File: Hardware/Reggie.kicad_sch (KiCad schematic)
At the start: 39 parts, among them J1 RBUS, U1 ESP32-S3, Y1 R940000171

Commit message: Updated connections
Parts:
- added R62: R, symbol Device:R
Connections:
- net GND: now also R62.2
- net VSPI_MOSI: now reaches U1.39 (GPIO34)
- net VSPI_MISO: now reaches U1.40 (GPIO35)
- net VSPI_SCLK: now reaches U1.41 (GPIO36)
- net BUCK_EN: now reaches U1.42 (GPIO37)
- net BuckPGOOD: now reaches U1.43 (GPIO38)
- net BuckPGOOD: now also R62.1
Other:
- sheet Buck ports: added BUCK_EN, PGOOD; removed none
- sheet SD ports: added SD1_CS, SD_DET, SD_Pow, VSPI_MISO, VSPI_MOSI, VSPI_SCLK; removed none

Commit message: Updated connections
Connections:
- net BUCK_EN: now also U1.37 (SPICLK_P/GPIO47); no longer U1.42 (GPIO37)
- net BuckPGOOD: now also U1.36 (SPICLK_N/GPIO48); no longer U1.43 (GPIO38)
- net SD1_CS: now also U1.42 (GPIO37)
- net SD_DET: now also U1.43 (GPIO38)
- net SD_EN: now also U1.51 (GPIO45)
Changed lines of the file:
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@@
 	(wire
 		(pts
-			(xy 135.89 100.33) (xy 142.24 100.33)
+			(xy 135.89 105.41) (xy 139.7 105.41)
+		)
+		(stroke
+			(width 0)
+			(type default)
+		)
+	)
+	(wire
+		(pts
+			(xy 135.89 100.33) (xy 139.7 100.33)
 		)
 		(stroke
@@
 	(wire
 		(pts
+			(xy 135.89 110.49) (xy 139.7 110.49)
+		)
+		(stroke
+			(width 0)
+			(type default)
+		)
+	)
+	(wire
+		(pts
 			(xy 128.27 25.4) (xy 128.27 26.67)
 		)
@@
 	(wire
 		(pts
+			(xy 135.89 115.57) (xy 139.7 115.57)
+		)
+		(stroke
+			(width 0)
+			(type default)
+		)
+	)
+	(wire
+		(pts
 			(xy 29.21 135.89) (xy 34.29 135.89)
 		)
@@
 	(wire
 		(pts
+			(xy 135.89 107.95) (xy 139.7 107.95)
+		)
+		(stroke
+			(width 0)
+			(type default)
+		)
+	)
+	(wire
+		(pts
 			(xy 27.94 21.59) (xy 30.48 21.59)
 		)
@@
 	(wire
 		(pts
-			(xy 135.89 107.95) (xy 144.78 107.95)
-		)
-		(stroke
-			(width 0)
-			(type default)
-		)
-	)
-	(wire
-		(pts
 			(xy 39.37 30.48) (xy 39.37 40.64)
 		)
@@
 	(wire
 		(pts
-			(xy 135.89 105.41) (xy 144.78 105.41)
-		)
-		(stroke
-			(width 0)
-			(type default)
-		)
-	)
-	(wire
-		(pts
 			(xy 199.39 116.84) (xy 204.47 116.84)
 		)
@@
 	(wire
 		(pts
-			(xy 135.89 102.87) (xy 143.51 102.87)
+			(xy 135.89 102.87) (xy 139.7 102.87)
 		)
 		(stroke
@@
 	(wire
 		(pts
+			(xy 135.89 118.11) (xy 139.7 118.11)
+		)
+		(stroke
+			(width 0)
+			(type default)
+		)
+	)
+	(wire
+		(pts
 			(xy 167.64 127) (xy 167.64 132.08)
 		)
@@
 	(wire
 		(pts
-			(xy 135.89 97.79) (xy 140.97 97.79)
+			(xy 135.89 97.79) (xy 139.7 97.79)
 		)
 		(stroke
@@
 	)
 	(label "VSPI_SCLK"
-		(at 143.51 102.87 0)
+		(at 139.7 102.87 0)
 		(effects
 			(font
@@
 		)
 	)
+	(label "SD_EN"
+		(at 139.7 110.49 0)
+		(effects
+			(font
+				(size 1.27 1.27)
+			)
+			(justify left bottom)
+		)
+	)
 	(label "Data-"
 		(at 99.06 162.56 0)
@@
 		)
 	)
+	(label "SD_DET"
+		(at 139.7 107.95 0)
+		(effects
+			(font
+				(size 1.27 1.27)
+			)
+			(justify left bottom)
+		)
+	)
 	(label "BOOT"
 		(at 59.69 110.49 0)
@@
 	)
 	(label "BuckPGOOD"
-		(at 144.78 107.95 0)
+		(at 139.7 115.57 0)
 		(effects
 			(font
@@
 	)
 	(label "VSPI_MISO"
-		(at 142.24 100.33 0)
+		(at 139.7 100.33 0)
 		(effects
 			(font
@@
 		)
 	)
+	(label "SD1_CS"
+		(at 139.7 105.41 0)
+		(effects
+			(font
+				(size 1.27 1.27)
+			)
+			(justify left bottom)
+		)
+	)
 	(label "BUCK_EN"
-		(at 144.78 105.41 0)
+		(at 139.7 118.11 0)
 		(effects
 			(font
@@
 	)
 	(label "VSPI_MOSI"
-		(at 140.97 97.79 0)
-		(effects
-			(font
+		(at 139.7 97.79 0)
+		(effects
+			(font

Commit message: new TVS
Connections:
- net ADS_DRDY: now reaches U1.10 (GPIO5/ADC1_CH4)
- net ADS_CLK: now reaches U1.11 (GPIO6/ADC1_CH5)
- net T_FAULT: now reaches U1.12 (GPIO7/ADC1_CH6)
- net T_DRDY: now reaches U1.13 (GPIO8/ADC1_CH7)
- net ADS_CS: now reaches U1.23 (GPIO17/ADC2_CH6/DAC_2)
- net T_CS: now reaches U1.27 (GPIO21)
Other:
- sheet Pressure ports: added ADS_CLK, ADS_CS0, ADS_DRDY, ADS_MISO, ADS_MOSI, ADS_SCLK; removed none
- sheet Thermocouple ports: added CS, DRDY, FAULT, MISO, MOSI, SCLK; removed none

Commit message: 2nd review of schematic
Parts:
- renumbered C13 to C12, C14 to C13, JP2 to JP1, JP3 to JP2, R5 to R3, R18 to R4, R3 to R5, R4 to R6, R6 to R7, R7 to R8, R62 to R9, TP9 to TP1, TP10 to TP2
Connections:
- net T_CS1: now reaches U1.45 (MTDO/JTAG/GPIO40)
- net T_FAULT1: now reaches U1.47 (MTDI/JTAG/GPIO41)
- net T_DRDY1: now reaches U1.48 (MTMS/JTAG/GPIO42)
- net T_CS renamed T_CS0
- net T_DRDY renamed T_DRDY0
- net T_FAULT renamed T_FAULT0
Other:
- sheet Thermocouple ports: added CS0, CS1, DRDY0, DRDY1, FAULT0, FAULT1; removed CS, DRDY, FAULT

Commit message: pcb update
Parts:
- R9: footprint (none) -> Resistor_SMD:R_0402_1005Metric
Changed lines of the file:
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@@
 			)
 		)
-		(property "Footprint" ""
+		(property "Footprint" "Resistor_SMD:R_0402_1005Metric"
 			(at 242.062 115.57 90)
 			(effects

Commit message: pcb and schematic update
Found all footprints including J3, pressure controller, tvs diode. PCB infrastructure update
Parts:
- R9: value R -> 18k
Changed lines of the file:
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@@
 			)
 		)
-		(property "Value" "R"
+		(property "Value" "18k"
 			(at 246.38 116.8399 0)
 			(effects

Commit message: PCB update
packing update
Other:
- sheet Ldo renamed Sensor Power
- sheet Sensor Power: file ldo.kicad_sch -> Sensor_Power.kicad_sch
- sheet Sensor Power ports: added 12V, 5V; removed none
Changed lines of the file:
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@@
 	(wire
 		(pts
+			(xy 256.54 52.07) (xy 261.62 52.07)
+		)
+		(stroke
+			(width 0)
+			(type default)
+		)
+	)
+	(wire
+		(pts
+			(xy 256.54 57.15) (xy 264.16 57.15)
+		)
+		(stroke
+			(width 0)
+			(type default)
+		)
+	)
+	(wire
+		(pts
 			(xy 53.34 191.77) (xy 45.72 191.77)
 		)
@@
 	(wire
 		(pts
+			(xy 261.62 50.8) (xy 261.62 52.07)
+		)
+		(stroke
+			(width 0)
+			(type default)
+		)
+	)
+	(wire
+		(pts
 			(xy 143.51 127) (xy 156.21 127)
 		)
@@
 	(wire
 		(pts
+			(xy 264.16 55.88) (xy 264.16 57.15)
+		)
+		(stroke
+			(width 0)
+			(type default)
+		)
+	)
+	(wire
+		(pts
 			(xy 189.23 92.71) (xy 193.04 92.71)
 		)
@@
 	)
 	(symbol
+		(lib_id "power:+5V")
+		(at 261.62 50.8 0)
+		(unit 1)
+		(exclude_from_sim no)
+		(in_bom yes)
+		(on_board yes)
+		(dnp no)
+		(fields_autoplaced yes)
+		(property "Reference" "#PWR098"
+			(at 261.62 54.61 0)
+			(effects
+				(font
+					(size 1.27 1.27)
+				)
+				(hide yes)
+			)
+		)
+		(property "Value" "+5V"
+			(at 261.62 45.72 0)
+			(effects
+				(font
+					(size 1.27 1.27)
+				)
+			)
+		)
+		(property "Footprint" ""
+			(at 261.62 50.8 0)
+			(effects
+				(font
+					(size 1.27 1.27)
+				)
+				(hide yes)
+			)
+		)
+		(property "Datasheet" ""
+			(at 261.62 50.8 0)
+			(effects
+				(font
+					(size 1.27 1.27)
+				)
+				(hide yes)
+			)
+		)
+		(property "Description" "Power symbol creates a global label with name \"+5V\""
+			(at 261.62 50.8 0)
+			(effects
+				(font
+					(size 1.27 1.27)
+				)
+				(hide yes)
+			)
+		)
+		(pin "1"
+		)
+		(instances
+			(project ""
+				(path "/7db990e4-92e1-4f99-b4d2-435bbec1ba83"
+					(reference "#PWR098")
+					(unit 1)
+				)
+			)
+		)
+	)
+	(symbol
 		(lib_id "power:GND")
 		(at 34.29 140.97 0)
@@
 	)
 	(symbol
+		(lib_id "power:+12V")
+		(at 264.16 55.88 0)
+		(unit 1)
+		(exclude_from_sim no)
+		(in_bom yes)
+		(on_board yes)
+		(dnp no)
+		(fields_autoplaced yes)
+		(property "Reference" "#PWR0148"
+			(at 264.16 59.69 0)
+			(effects
+				(font
+					(size 1.27 1.27)
+				)
+				(hide yes)
+			)
+		)
+		(property "Value" "+12V"
+			(at 264.16 50.8 0)
+			(effects
+				(font
+					(size 1.27 1.27)
+				)
+			)
+		)
+		(property "Footprint" ""
+			(at 264.16 55.88 0)
+			(effects
+				(font
+					(size 1.27 1.27)
+				)
+				(hide yes)
+			)
+		)
+		(property "Datasheet" ""
+			(at 264.16 55.88 0)
+			(effects
+				(font
+					(size 1.27 1.27)
+				)
+				(hide yes)
+			)
+		)
+		(property "Description" "Power symbol creates a global label with name \"+12V\""
+			(at 264.16 55.88 0)
+			(effects
+				(font
+					(size 1.27 1.27)
+				)
+				(hide yes)
+			)
+		)
+		(pin "1"
+		)
+		(instances
+			(project ""
+				(path "/7db990e4-92e1-4f99-b4d2-435bbec1ba83"
+					(reference "#PWR0148")
+					(unit 1)
+				)
+			)
+		)
+	)
+	(symbol
 		(lib_id "Connector:TestPoint")
 		(at 30.48 59.69 90)
@@
 	)
 	(sheet
-		(at 233.045 46.99)
+		(at 234.95 46.99)
 		(size 21.59 15.24)
 		(exclude_from_sim no)
@@
 			(color 0 0 0 0.0000)
 		)
-		(property "Sheetname" "Ldo"
-			(at 233.045 46.2784 0)
+		(property "Sheetname" "Sensor Power"
+			(at 234.95 46.2784 0)
 			(effects
 				(font
@@
 			)
 		)
-		(property "Sheetfile" "ldo.kicad_sch"
-			(at 233.045 62.8146 0)
+		(property "Sheetfile" "Sensor_Power.kicad_sch"
+			(at 234.95 62.8146 0)
 			(effects
 				(font
@@
 			)
 		)
+		(pin "5V" output
+			(at 256.54 52.07 0)
+			(effects
+				(font
+					(size 1.27 1.27)
+				)
+				(justify right)
+			)
+		)
+		(pin "12V" output
+			(at 256.54 57.15 0)
+			(effects
+				(font
+					(size 1.27 1.27)
+				)
+				(justify right)
+			)
+		)

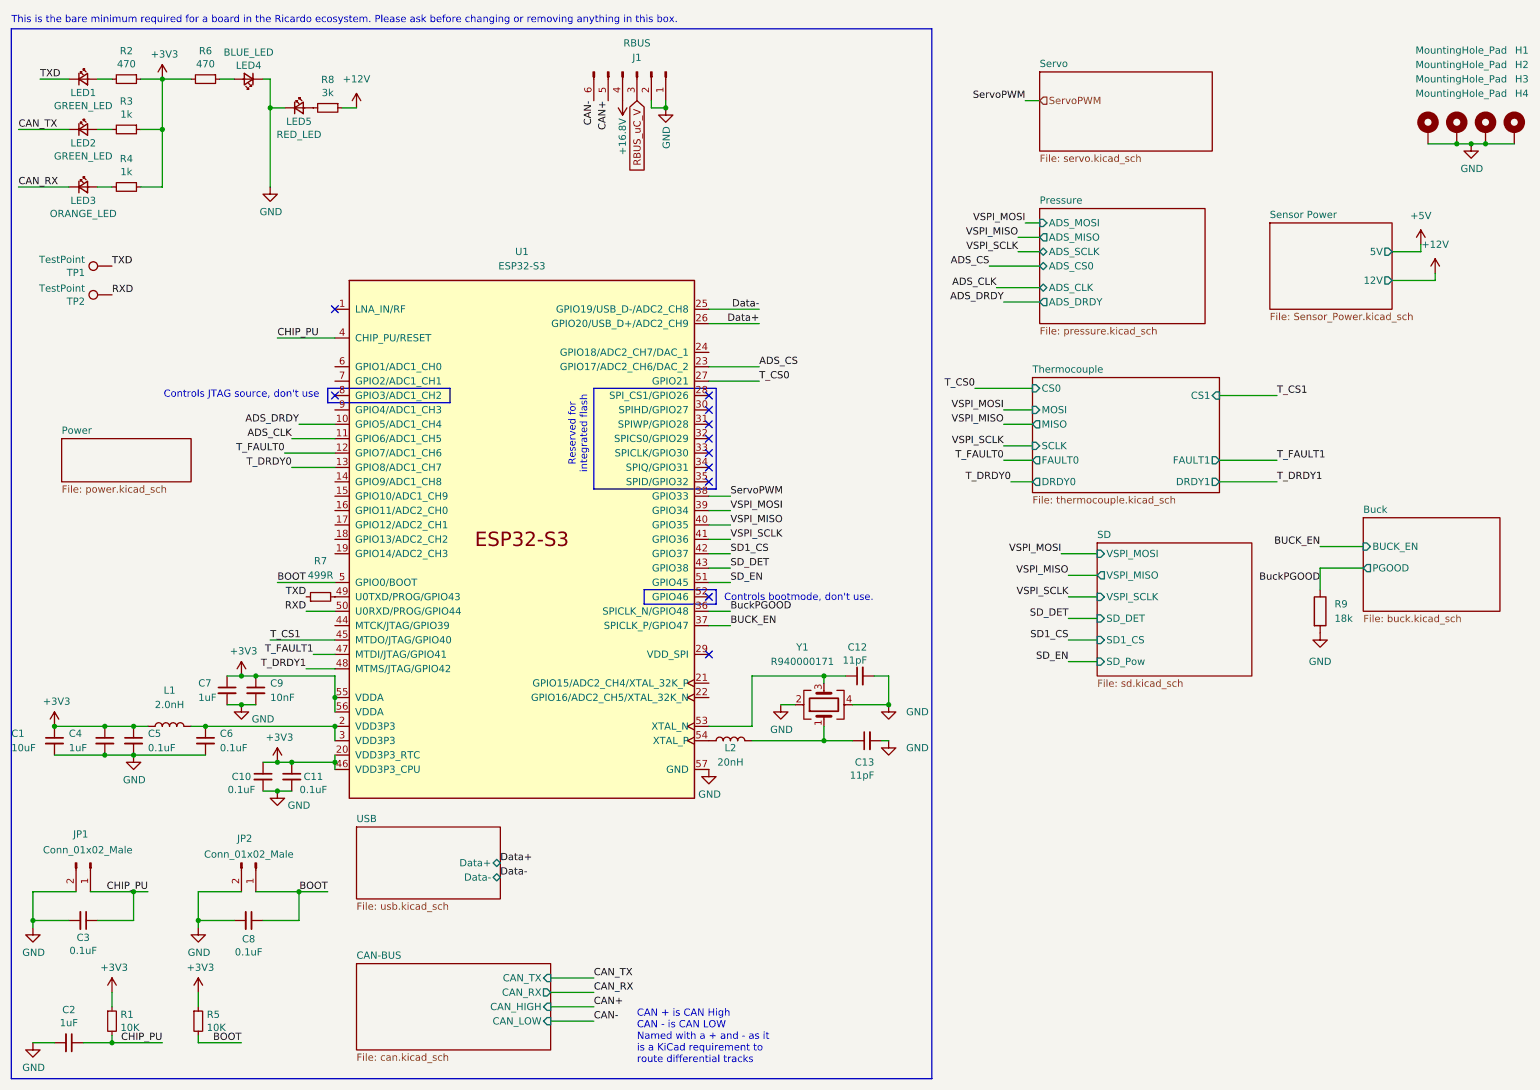
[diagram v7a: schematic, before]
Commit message: schematic changes and updated tvs footprints
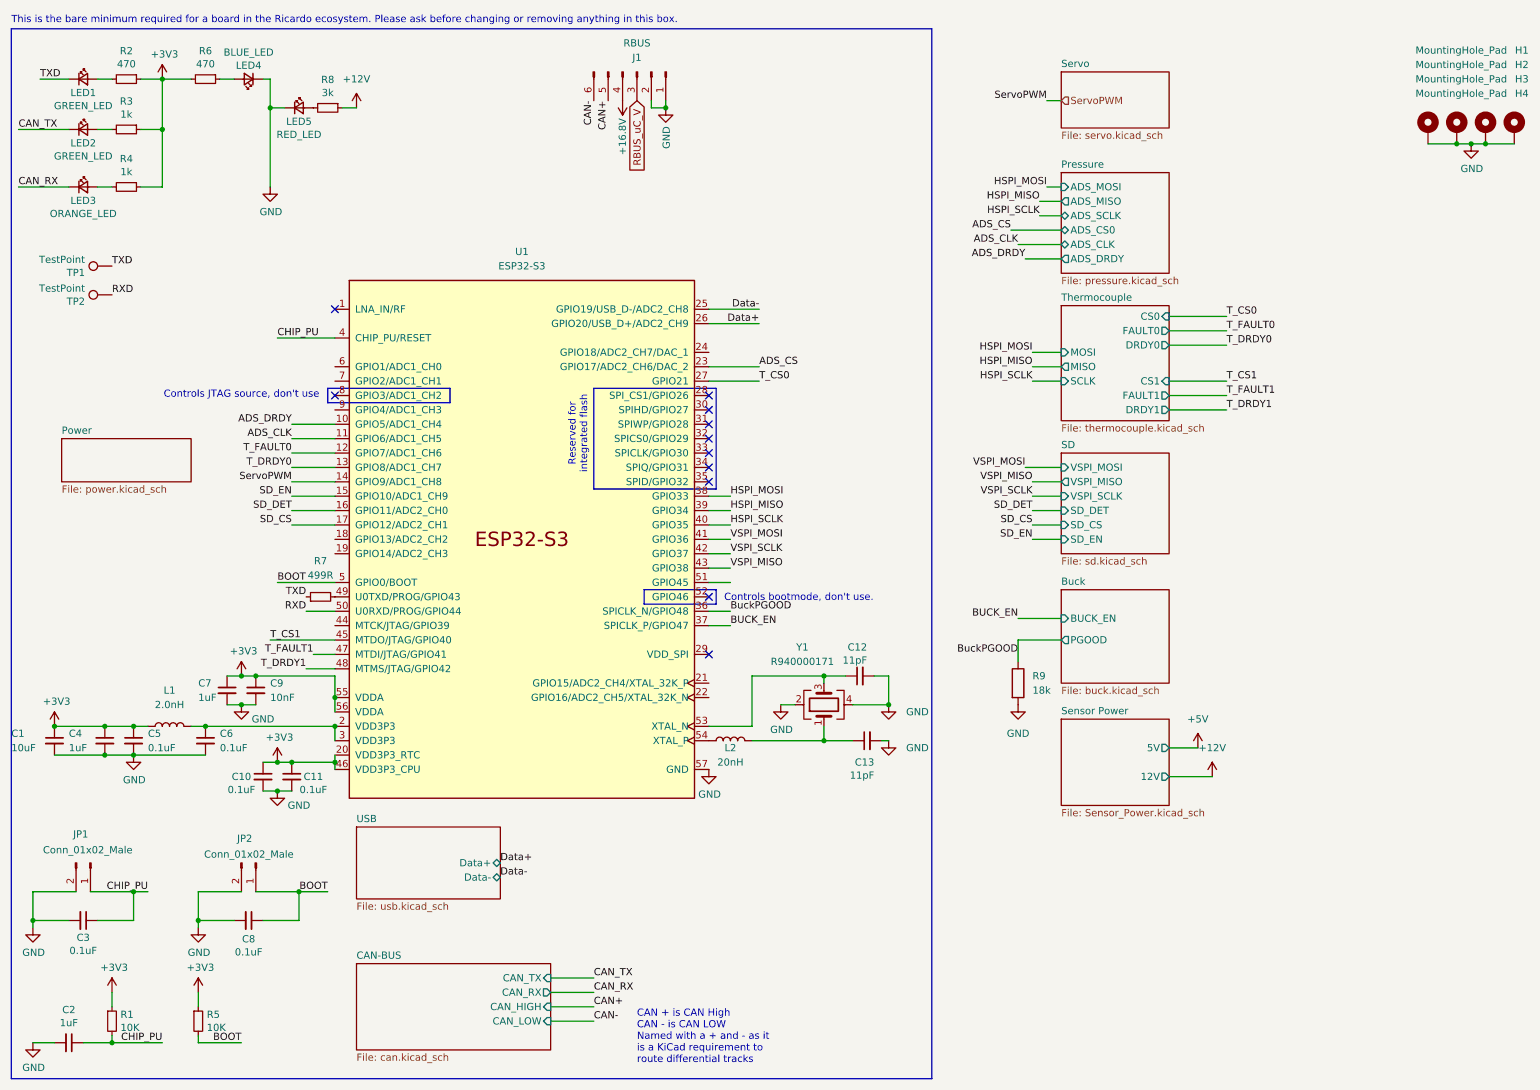
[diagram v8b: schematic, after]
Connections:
- net SD1_CS is gone; now on net VSPI_SCLK: U1.42 (GPIO37)
- net SD_DET: now also U1.16 (GPIO11/ADC2_CH0); no longer U1.43 (GPIO38)
- net SD_EN: now also U1.15 (GPIO10/ADC1_CH9); no longer U1.51 (GPIO45)
- net ServoPWM: now also U1.14 (GPIO9/ADC1_CH8); no longer U1.38 (GPIO33)
- net VSPI_MISO: now also U1.43 (GPIO38); no longer U1.40 (GPIO35)
- net VSPI_MOSI: now also U1.41 (GPIO36); no longer U1.39 (GPIO34)
- net VSPI_SCLK: no longer U1.41 (GPIO36)
- net SD_CS: now reaches U1.17 (GPIO12/ADC2_CH1)
- new net HSPI_MISO: U1.39 (GPIO34)
- new net HSPI_MOSI: U1.38 (GPIO33)
- new net HSPI_SCLK: U1.40 (GPIO35)
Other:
- sheet SD ports: added SD_CS, SD_EN; removed SD1_CS, SD_Pow
- moved on the sheet: R9
